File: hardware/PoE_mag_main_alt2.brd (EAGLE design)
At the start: 149.9 x 124.5 mm, 119 parts, among them IC1 LD1117S33TR, IC10 PCA9517A, IC2 DS1338, IC3 74LVC1T45SOT23-HAND, IC4 ATMEGA1284, IC5 MCP2200, IC6 TSR 1-2450, IC7 74LVC1T45SOT23-HAND, IC8 74LVC1T45SOT23-HAND, IC9 74LVC1T45SOT23-HAND, Q1 BSS138, Q3 BUK98150-55A, X1 PWR, X2 JTAG, X3 USB, X4 CONN-SMATHD, X5 UFL, X6 MICRO-SD-SOCKETHIROSE-DM3D, X7 RJ45, X8 RJ11, X9 22-23-2021, Y1 32k768, Y2 16MHz, Y3 12MHz

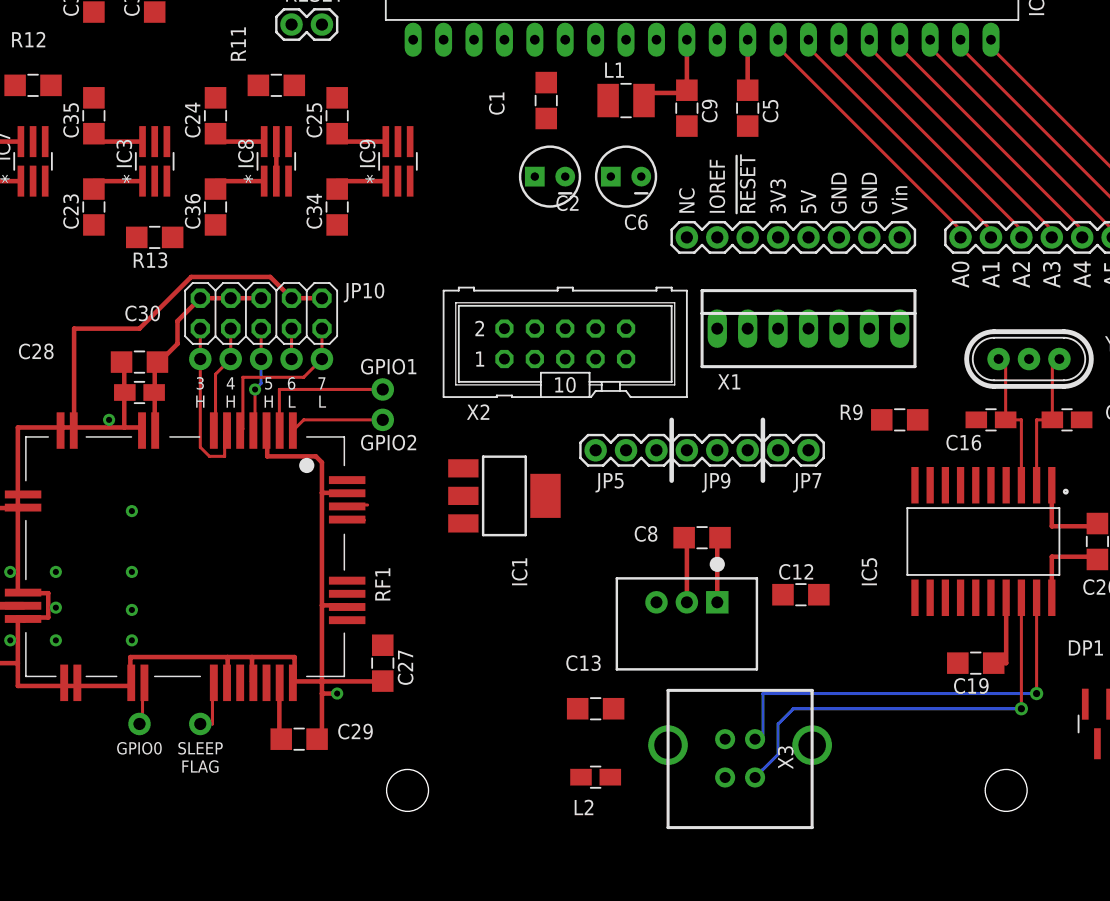
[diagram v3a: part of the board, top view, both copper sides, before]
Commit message: Use TO220 package of LD1117
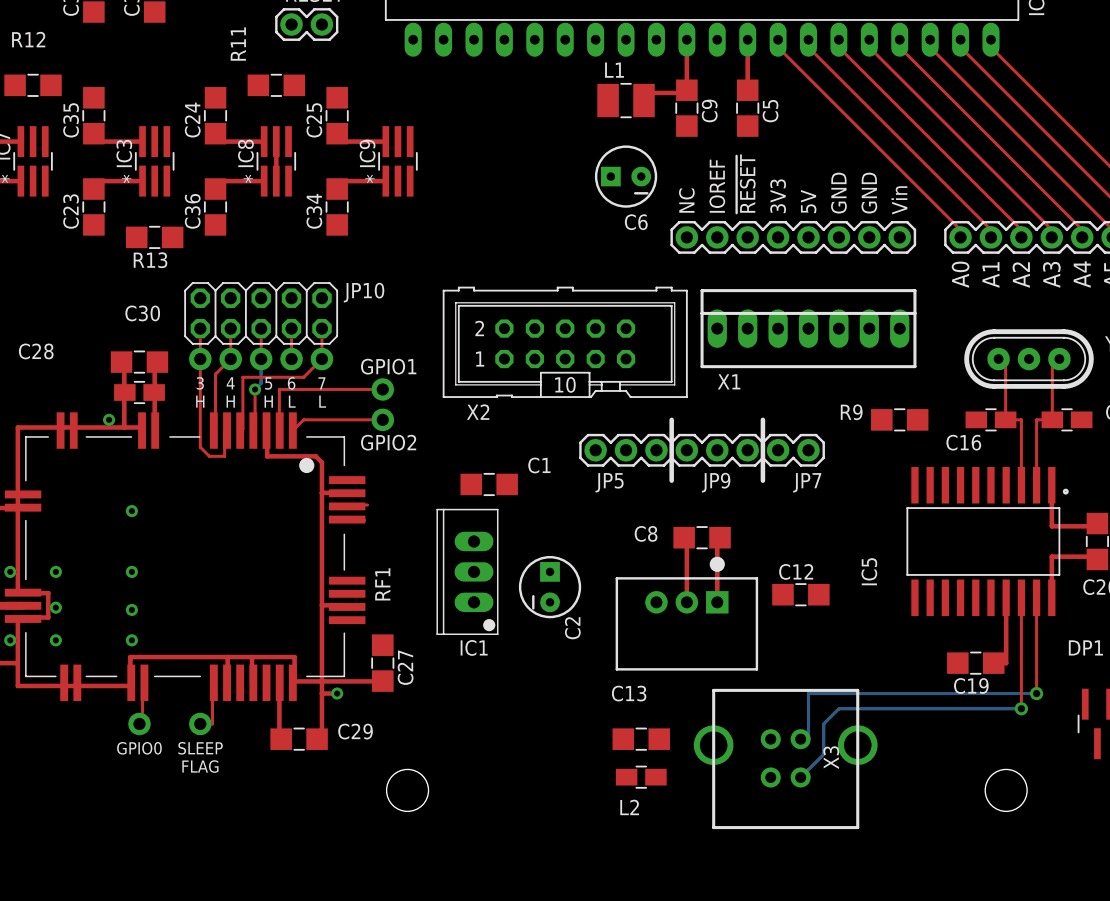
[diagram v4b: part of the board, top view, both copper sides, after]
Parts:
- IC1: device SteveMarple:SOT223-HAND -> SteveMarple:TO220
- moved C2 34.3 mm to (69.8, 16.5), turned to 90 degrees
- moved C1 32.4 mm to (64.8, 25.1), turned to 0 degrees
- moved IC1 6.84 mm to (63.5, 17.8), turned to 90 degrees
- moved C13 4.58 mm to (77.5, 3.81)
- moved L2 3.81 mm to (77.5, 0.64)
- moved X3 3.81 mm to (89.5, 3.81)
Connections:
- net +3V3: no longer IC1.4
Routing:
- net GND: track 226.2 -> 194.8 mm
- net +3V3: track 49.2 -> 37.8 mm
- net USB_D-: track 35.4 -> 31.6 mm
- net USB_D+: track 35.3 -> 31.5 mm

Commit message: Board layout changes
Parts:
- IC1: value LD1117S33TR -> LD1117V33
- moved C6 56.8 mm to (119.4, 87.6), turned to 270 degrees
- moved C8 12.1 mm to (90.8, 11.7)
- moved C10 7.24 mm to (80.6, 87.6), turned to 180 degrees
- moved C11 7.10 mm to (74.3, 87.6), turned to 0 degrees
- moved C7 2.84 mm to (87.0, 81.9)
- moved Y2 1.80 mm to (77.5, 83.2)
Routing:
- net GND: track 194.8 -> 211.0 mm
- net VIN: track 5.08 -> 0.00 mm
- net N$2: track 8.04 -> 11.2 mm
- net N$1: track 8.04 -> 11.2 mm
- net VCC: track 37.9 -> 40.5 mm
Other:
- board text added: "GPS ANTENNA"
- board text added: "JP4: PPS PIN"
- board text added: "JP5: MCU OPERATION"
- board text added: "JP9: POWER SOURCE"
- board text added: "MCU"
- board text added: "PPS 6"
- board text added: "PPS 7"
- board text added: "PWR SRC"
- board text added: "USB"
- board text added: "VIN"
- board text added: "µSD: 3V3 operation only"
